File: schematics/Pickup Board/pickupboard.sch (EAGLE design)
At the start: 1 part, among them IC1 A1202LH

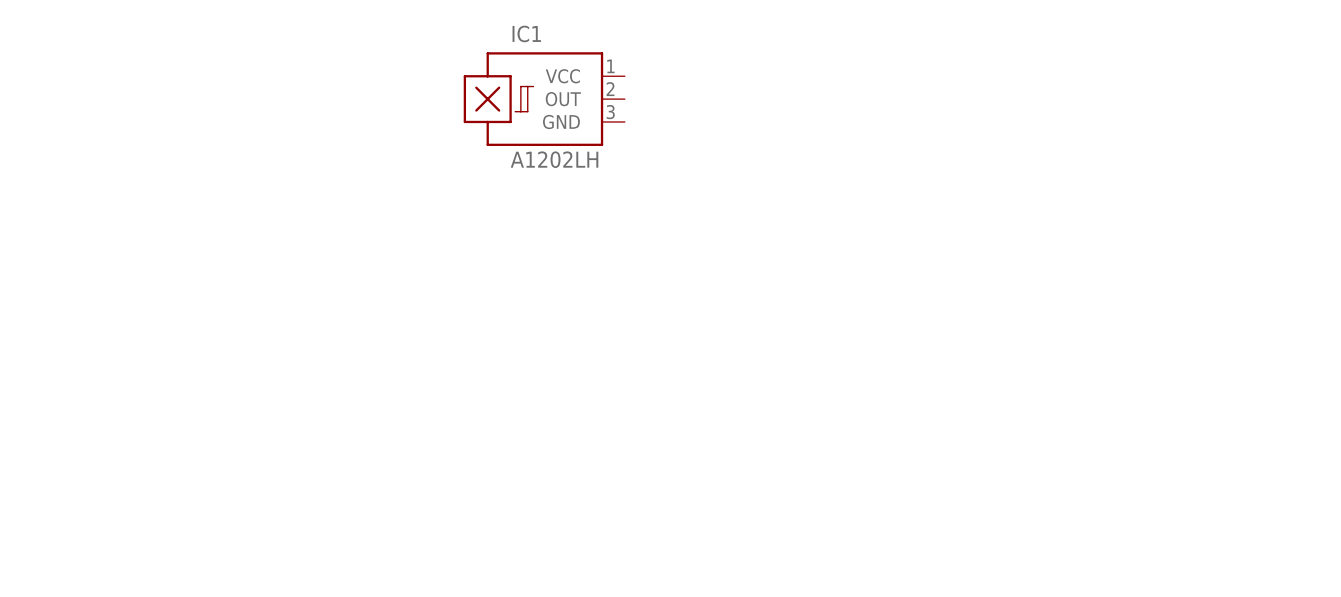
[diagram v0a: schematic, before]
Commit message: Added named inductors to Eagle schematic
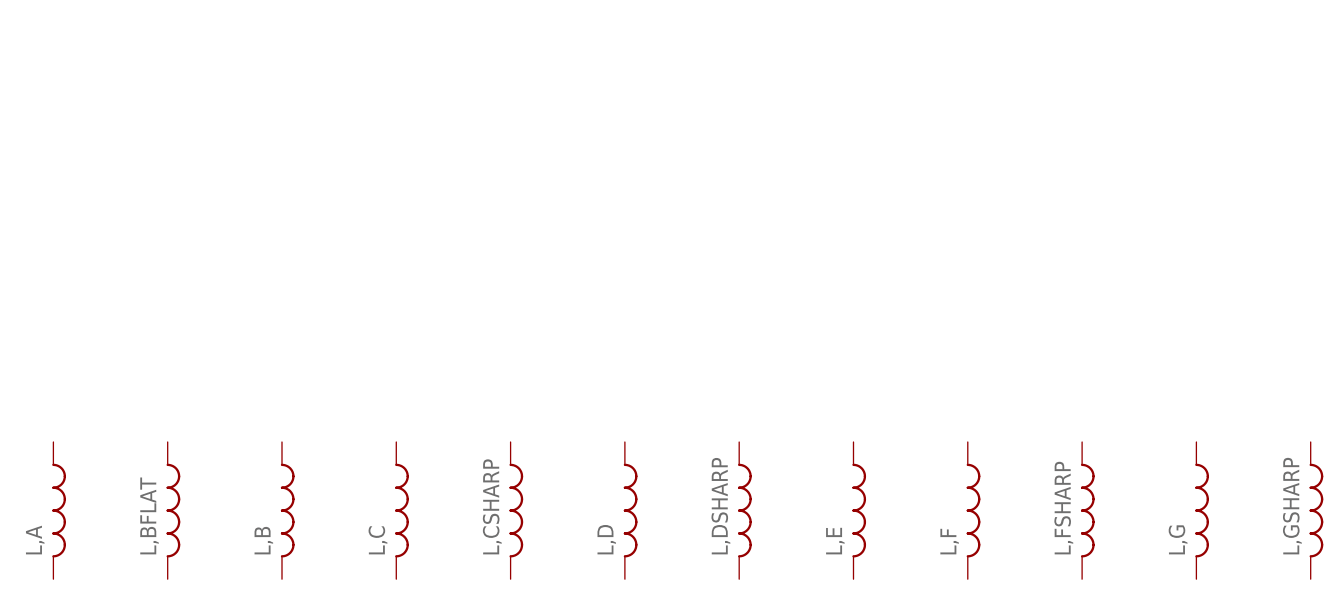
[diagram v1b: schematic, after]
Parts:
- removed IC1: A1202LH, allegro:A1202LH
- added L,A, L,B, L,BFLAT, L,C, L,CSHARP, L,D, L,DSHARP, L,E, L,F, L,FSHARP, L,G, L,GSHARP: (no value), resistor:L-US0204/5
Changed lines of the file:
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@@
 <layer number="97" name="Info" color="7" fill="1" visible="yes" active="yes"/>
 <layer number="98" name="Guide" color="6" fill="1" visible="yes" active="yes"/>
+<layer number="99" name="SpiceOrder" color="5" fill="1" visible="yes" active="yes"/>
 </layers>
 <schematic xreflabel="%F%N/%S.%C%R" xrefpart="/%S.%C%R">
@@
 </classes>
 <parts>
-<part name="IC1" library="allegro" deviceset="A12*?" device="LH" technology="02"/>
+<part name="L,A" library="resistor" deviceset="L-US" device="0204/5"/>
+<part name="L,BFLAT" library="resistor" deviceset="L-US" device="0204/5"/>
+<part name="L,B" library="resistor" deviceset="L-US" device="0204/5"/>
+<part name="L,C" library="resistor" deviceset="L-US" device="0204/5"/>
+<part name="L,CSHARP" library="resistor" deviceset="L-US" device="0204/5"/>
+<part name="L,D" library="resistor" deviceset="L-US" device="0204/5"/>
+<part name="L,DSHARP" library="resistor" deviceset="L-US" device="0204/5"/>
+<part name="L,E" library="resistor" deviceset="L-US" device="0204/5"/>
+<part name="L,F" library="resistor" deviceset="L-US" device="0204/5"/>
+<part name="L,FSHARP" library="resistor" deviceset="L-US" device="0204/5"/>
+<part name="L,G" library="resistor" deviceset="L-US" device="0204/5"/>
+<part name="L,GSHARP" library="resistor" deviceset="L-US" device="0204/5"/>
 </parts>
 <sheets>
@@
 </plain>
 <instances>
-<instance part="IC1" gate="G$1" x="50.8" y="58.42"/>
+<instance part="L,A" gate="G$1" x="-5.08" y="12.7"/>
+<instance part="L,BFLAT" gate="G$1" x="7.62" y="12.7"/>
+<instance part="L,B" gate="G$1" x="20.32" y="12.7"/>
+<instance part="L,C" gate="G$1" x="33.02" y="12.7"/>
+<instance part="L,CSHARP" gate="G$1" x="45.72" y="12.7"/>
+<instance part="L,D" gate="G$1" x="58.42" y="12.7"/>
+<instance part="L,DSHARP" gate="G$1" x="71.12" y="12.7"/>
+<instance part="L,E" gate="G$1" x="83.82" y="12.7"/>
+<instance part="L,F" gate="G$1" x="96.52" y="12.7"/>
+<instance part="L,FSHARP" gate="G$1" x="109.22" y="12.7"/>
+<instance part="L,G" gate="G$1" x="121.92" y="12.7"/>
+<instance part="L,GSHARP" gate="G$1" x="134.62" y="12.7"/>
 </instances>
 <busses>
